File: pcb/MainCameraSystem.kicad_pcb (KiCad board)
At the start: 4 copper layers, 40 x 40 mm, 57 parts, among them J1 FFC2B28-24-G, J2 Debug, J3 0472192001, SW1 B3U-1000P, SW2 B3U-1000P, U1 STM32H533VET6, U2 TLV70028DDCR, U3 TLV70015DDCR, Y1 ASV-24.000MHZ-EJ-T

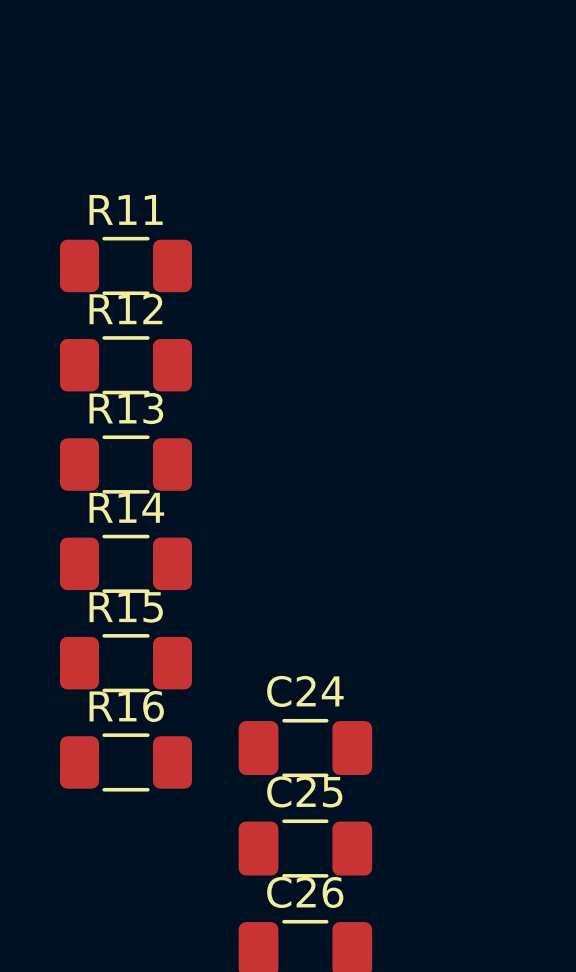
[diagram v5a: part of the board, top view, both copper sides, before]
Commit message: Removed series resistors for `uSD Connector` design block.
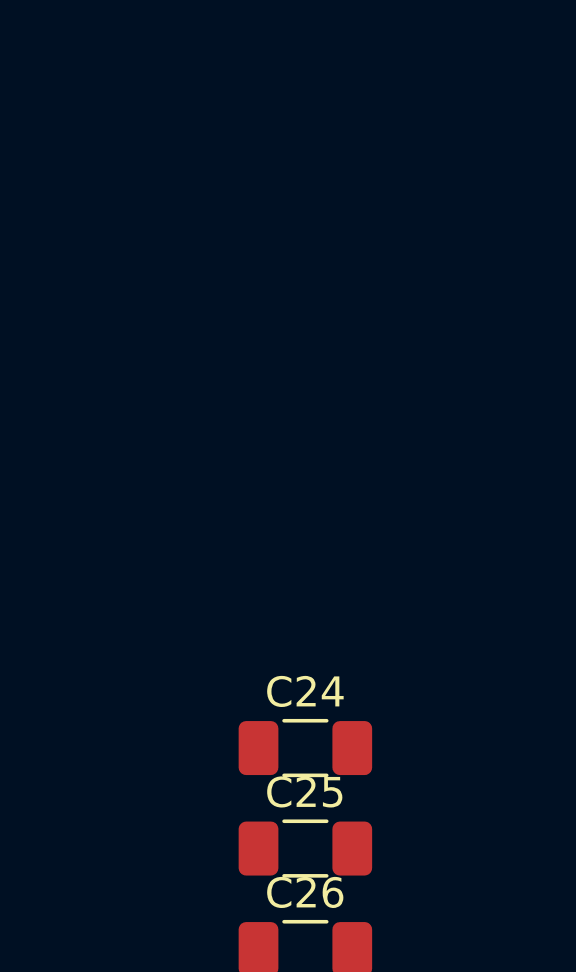
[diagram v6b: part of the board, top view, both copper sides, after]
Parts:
- removed R11, R12, R13, R14, R15, R16: R_Small, Resistor_SMD:R_1206_3216Metric_Pad1.30x1.75mm_HandSolder
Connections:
- J3 pad 1: Net-(J3-DAT2) -> sd_data_2
- J3 pad 2: Net-(J3-DAT3/CD) -> sd_data_3
- J3 pad 3: Net-(J3-CMD) -> sd_cmd
- J3 pad 5: Net-(J3-CLK) -> sd_clock
- J3 pad 7: Net-(J3-DAT0) -> sd_data_0
- J3 pad 8: Net-(J3-DAT1) -> sd_data_1

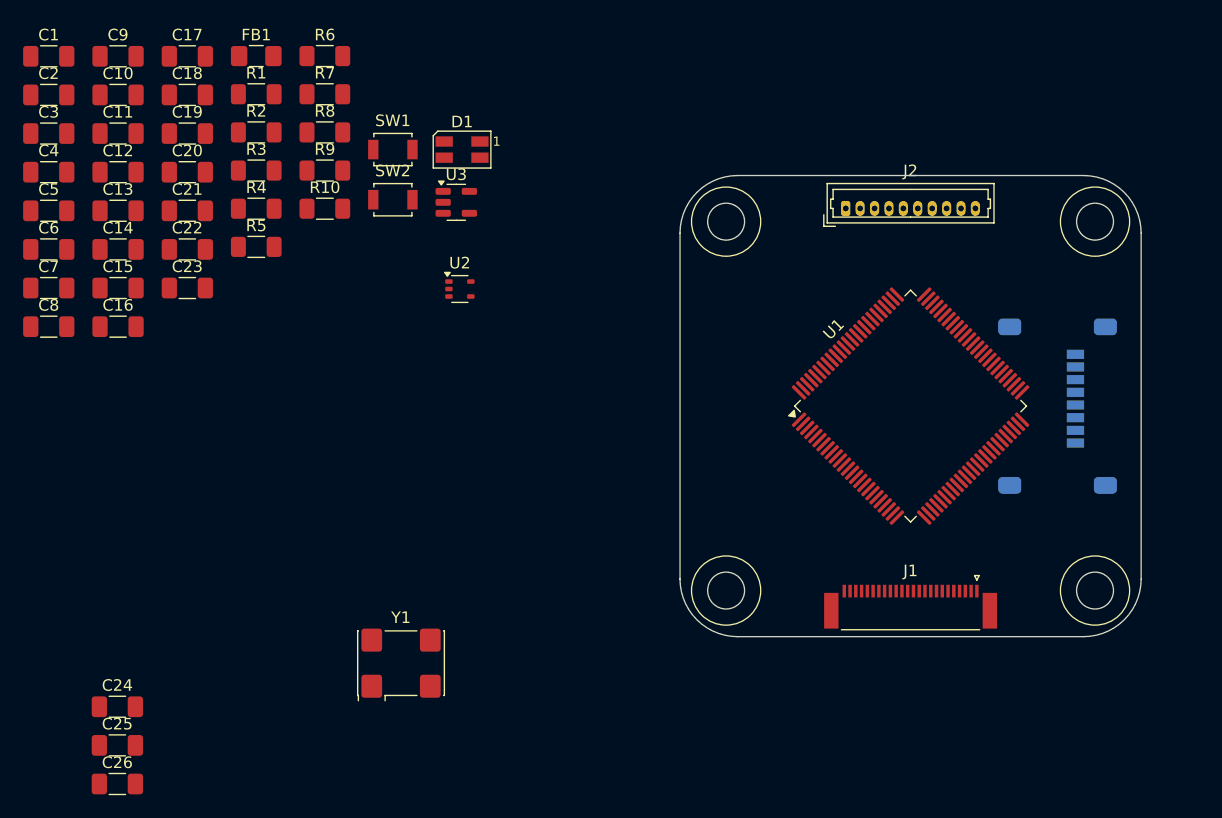
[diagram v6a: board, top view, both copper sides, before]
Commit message: Rough layout of components for `MainCameraSystem`.
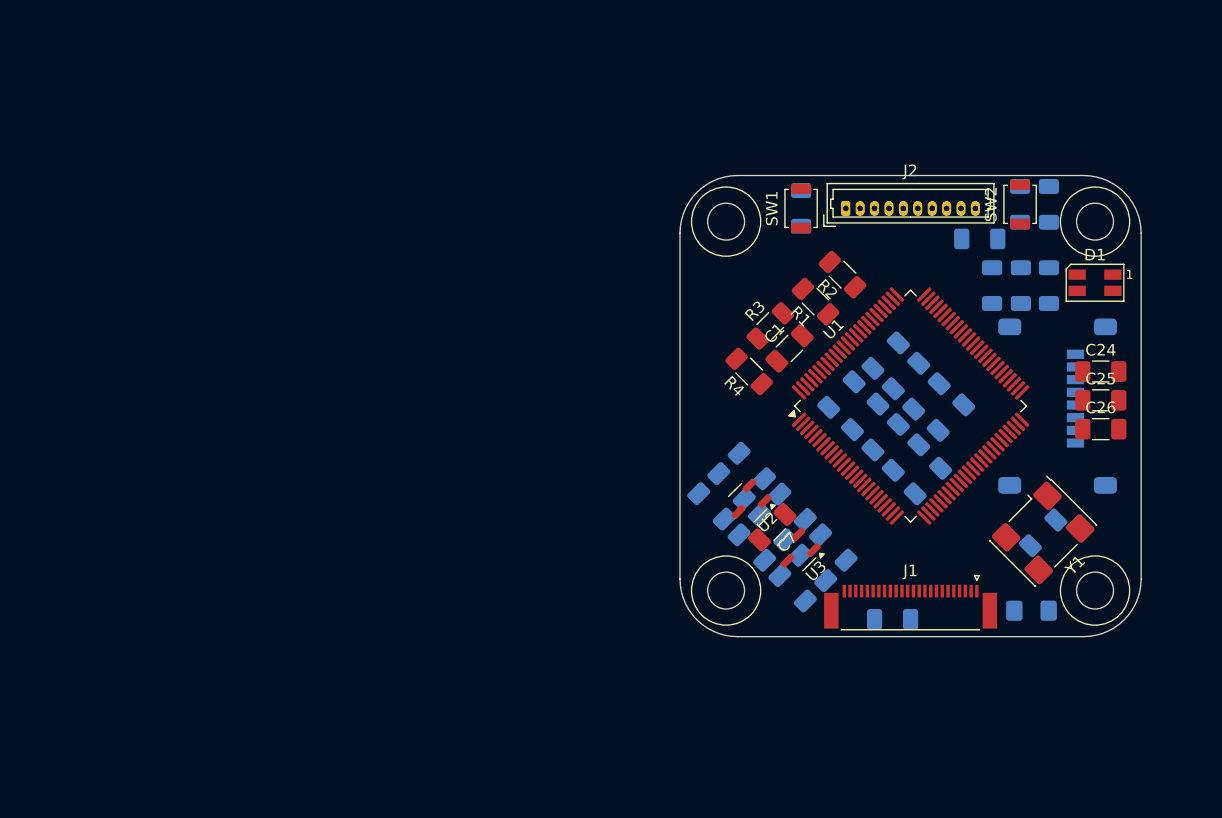
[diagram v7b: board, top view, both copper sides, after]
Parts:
- C10, C11, C12, C13, C14, C15, C16, C17, C18, C19, C2, C20, C21, C22, C23, C3, C4, C5, C6, C8, C9, FB1, R10, R5, R6, R7, R8, R9: moved to B.Cu
- U2: value TLV70028DDCR -> AP2127N-2.8TRG1; footprint Package_TO_SOT_SMD:SOT-353_SC-70-5 -> Package_TO_SOT_SMD:SOT-23-3
- U3: value TLV70015DDCR -> AP2127N-1.8; footprint Package_TO_SOT_SMD:SOT-23-5 -> Package_TO_SOT_SMD:SOT-23-3
- moved C26 90.7 mm to (166.5, 102.0)
- moved C5 90.7 mm to (161.5, 111.0), turned to 45 degrees
- moved C25 90.4 mm to (166.5, 99.5)
- moved C24 90.1 mm to (166.5, 97.0)
- moved C2 86.2 mm to (148.4, 118.5)
- moved FB1 82.7 mm to (160.5, 117.8), turned to 180 degrees
- moved C8 76.4 mm to (151.4, 99.2), turned to 45 degrees
- moved C12 75.2 mm to (151.5, 106.5), turned to -135 degrees
- moved C16 75.1 mm to (156.0, 85.5)
- moved C11 71.7 mm to (143.3, 112.3), turned to -45 degrees
- moved C9 71.5 mm to (147.8, 95.6), turned to 45 degrees
- moved C13 69.8 mm to (149.6, 97.4), turned to 45 degrees
- moved C1 69.1 mm to (139.5, 95.0), turned to 45 degrees
- moved C10 68.6 mm to (139.8, 108.7), turned to -45 degrees
- moved C23 67.2 mm to (153.5, 101.0), turned to -135 degrees
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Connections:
- U2 pad 1: +3.3V -> GND
- U2 pad 2: GND -> +2V8
- U3 pad 1: +3.3V -> GND
- U3 pad 2: GND -> +1V5

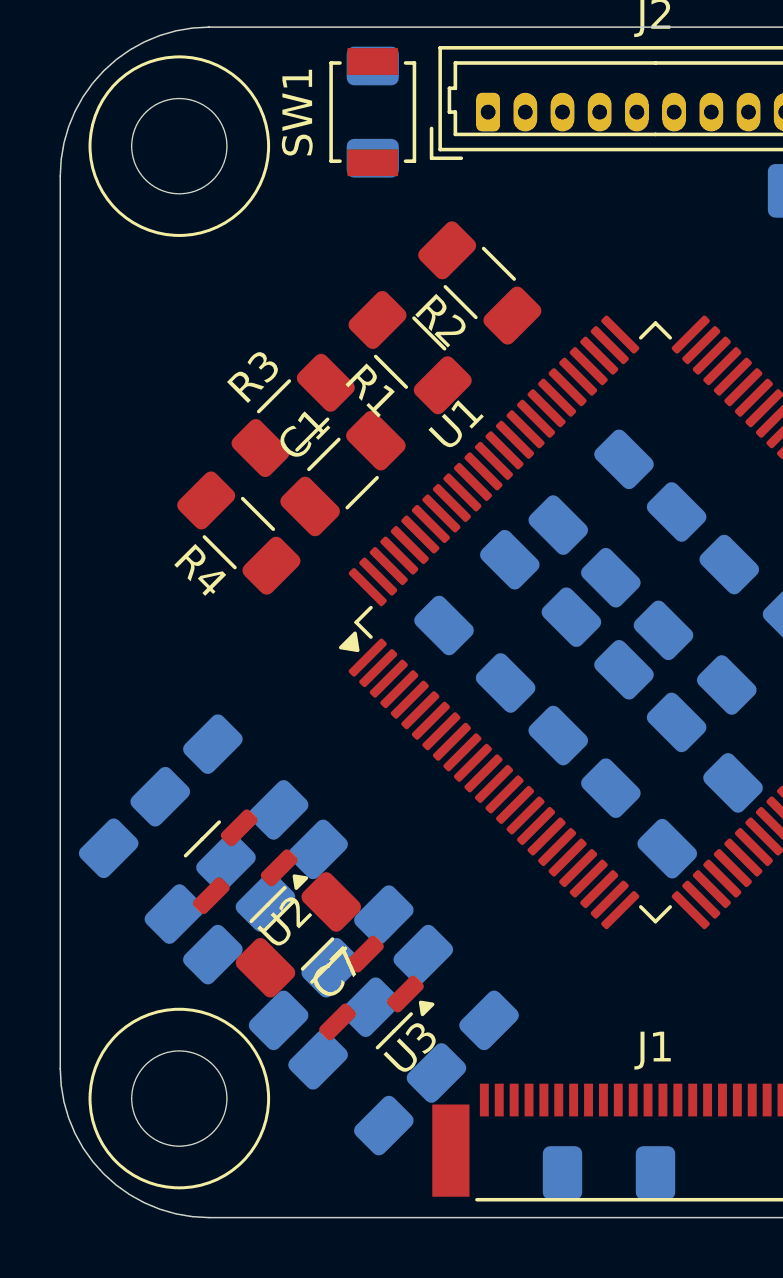
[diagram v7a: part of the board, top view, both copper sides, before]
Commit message: Added 4-pin connector for `MainCameraSystem`.
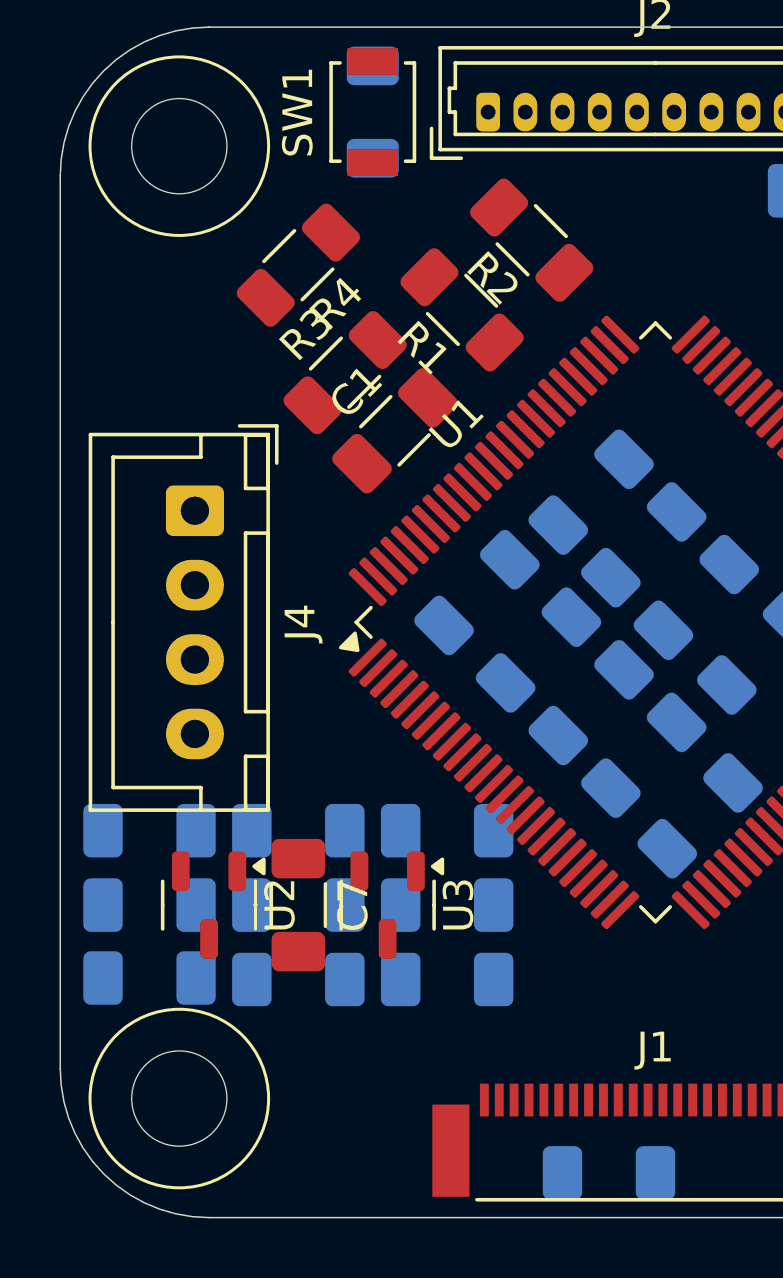
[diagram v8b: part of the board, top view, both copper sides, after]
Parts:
- added J4: B4B-XH-A, Connector_JST:JST_XH_B4B-XH-A_1x04_P2.50mm_Vertical, F.Cu at (134.5, 96.3)
- moved R4 9.22 mm to (138.0, 88.0), turned to -135 degrees
- moved C11 5.28 mm to (143.0, 107.0), turned to 0 degrees
- moved C15 4.99 mm to (143.0, 112.0), turned to 0 degrees
- moved C19 4.77 mm to (143.0, 109.5), turned to 0 degrees
- moved C6 3.70 mm to (133.0, 107.0), turned to 0 degrees
- moved C3 3.26 mm to (133.0, 112.0), turned to 0 degrees
- moved U3 3.24 mm to (141.0, 109.5), turned to -90 degrees
- moved C4 2.93 mm to (133.0, 109.5), turned to 0 degrees
- moved C10 2.48 mm to (138.0, 107.0), turned to 0 degrees
- moved R2 2.26 mm to (145.8, 87.2)
- moved R3 2.26 mm to (139.6, 91.6)
- moved C1 2.26 mm to (141.2, 93.6)
- moved R1 2.26 mm to (143.5, 89.5)
- moved C18 1.79 mm to (138.0, 112.0), turned to 0 degrees
- moved U2 1.42 mm to (135.0, 109.5), turned to -90 degrees
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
